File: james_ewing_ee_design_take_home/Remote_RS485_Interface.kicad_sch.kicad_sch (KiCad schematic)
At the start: 16 parts, among them J1 USB_B_Micro, J3 RJ45, U2 MCP2200-E-SS, U3 SN65176BDR, Y1 Resonator

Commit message: Updated
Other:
- note added: "Terminating Resistor"
- title: (none) -> Remote Interface Communication Circuit
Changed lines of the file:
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@@
 (kicad_sch (version 20230121) (generator eeschema)
   (paper "A4")
+  (title_block
+    (title "Remote Interface Communication Circuit")
+  )
   (junction (at 68.58 124.46) (diameter 0) (color 0 0 0 0)
   )
@@
     (stroke (width 0) (type default))
   )
+  (text "Terminating \nResistor" (at 123.19 152.4 0)
+    (effects (font (size 1.27 1.27)) (justify left bottom))
+  )
   (text "USB to UART Interface" (at 36.83 27.94 0)

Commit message: Updated Schematic
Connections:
- net 5V  renamed 5V_RI
- no-connect marks 8 -> 17
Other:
- note added: "TODO: Look into Reset Button Circuit for ESP8266"
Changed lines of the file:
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@@
   (junction (at 119.38 139.7) (diameter 0) (color 0 0 0 0)
   )
+  (no_connect (at 129.54 49.53))
   (no_connect (at 137.16 137.16))
   (no_connect (at 38.1 71.12))
   (no_connect (at 48.26 66.04))
+  (no_connect (at 129.54 64.77))
+  (no_connect (at 129.54 57.15))
   (no_connect (at 137.16 134.62))
+  (no_connect (at 129.54 52.07))
+  (no_connect (at 129.54 69.85))
   (no_connect (at 137.16 127))
   (no_connect (at 137.16 139.7))
   (no_connect (at 137.16 132.08))
+  (no_connect (at 129.54 46.99))
+  (no_connect (at 129.54 62.23))
+  (no_connect (at 129.54 67.31))
   (no_connect (at 137.16 129.54))
+  (no_connect (at 129.54 54.61))
   (wire (pts (xy 125.73 139.7) (xy 134.62 139.7))
     (stroke (width 0) (type default))
@@
     (stroke (width 0) (type default))
   )
+  (wire (pts (xy 130.81 59.69) (xy 129.54 59.69))
+    (stroke (width 0) (type default))
+  )
   (wire (pts (xy 74.93 146.05) (xy 69.85 146.05))
     (stroke (width 0) (type default))
@@
     (stroke (width 0) (type default))
   )
+  (wire (pts (xy 82.55 72.39) (xy 83.82 72.39))
+    (stroke (width 0) (type default))
+  )
   (wire (pts (xy 119.38 130.81) (xy 119.38 139.7))
     (stroke (width 0) (type default))
@@
     (stroke (width 0) (type default))
   )
+  (wire (pts (xy 132.08 74.93) (xy 129.54 74.93))
+    (stroke (width 0) (type default))
+  )
   (wire (pts (xy 72.39 48.26) (xy 72.39 46.99))
     (stroke (width 0) (type default))
@@
     (stroke (width 0) (type default))
   )
+  (wire (pts (xy 132.08 72.39) (xy 129.54 72.39))
+    (stroke (width 0) (type default))
+  )
   (wire (pts (xy 80.01 52.07) (xy 83.82 52.07))
+    (stroke (width 0) (type default))
+  )
+  (wire (pts (xy 82.55 77.47) (xy 83.82 77.47))
     (stroke (width 0) (type default))
   )
@@
     (effects (font (size 1.27 1.27)) (justify left bottom))
   )
+  (text "TODO: Look into Reset Button Circuit for ESP8266" (at 162.56 69.85 0)
+    (effects (font (size 1.27 1.27)) (justify left bottom))
+  )
   (text "12MHz Resonator for USB" (at 45.72 41.91 0)
     (effects (font (size 1.27 1.27)) (justify left bottom))
@@
     (effects (font (size 1.27 1.27)) (justify left bottom))
   )
-  (global_label "TX_RX_SEL" (shape input) (at 129.54 59.69 0) (fields_autoplaced)
+  (label "D_Plus" (at 48.26 60.96 0) (fields_autoplaced)
+    (effects (font (size 1.27 1.27)) (justify left bottom))
+  )
+  (label "D_Minus" (at 82.55 72.39 180) (fields_autoplaced)
+    (effects (font (size 1.27 1.27)) (justify right bottom))
+  )
+  (label "UART_TX" (at 55.88 151.13 180) (fields_autoplaced)
+    (effects (font (size 1.27 1.27)) (justify right bottom))
+  )
+  (label "D_Minus" (at 48.26 63.5 0) (fields_autoplaced)
+    (effects (font (size 1.27 1.27)) (justify left bottom))
+  )
+  (label "D_Plus" (at 82.55 77.47 180) (fields_autoplaced)
+    (effects (font (size 1.27 1.27)) (justify right bottom))
+  )
+  (label "TX_RX_SEL" (at 130.81 59.69 0) (fields_autoplaced)
+    (effects (font (size 1.27 1.27)) (justify left bottom))
+  )
+  (label "UART_TX" (at 132.08 72.39 0) (fields_autoplaced)
+    (effects (font (size 1.27 1.27)) (justify left bottom))
+  )
+  (label "UART_RX" (at 132.08 74.93 0) (fields_autoplaced)
+    (effects (font (size 1.27 1.27)) (justify left bottom))
+  )
+  (label "TX_RX_SEL" (at 58.42 146.05 180) (fields_autoplaced)
+    (effects (font (size 1.27 1.27)) (justify right bottom))
+  )
+  (label "UART_RX" (at 55.88 140.97 180) (fields_autoplaced)
+    (effects (font (size 1.27 1.27)) (justify right bottom))
+  )
+  (global_label "5V_RI" (shape input) (at 85.09 121.92 90) (fields_autoplaced)
     (effects (font (size 1.27 1.27)) (justify left))
-    (property "Intersheetrefs" "${INTERSHEET_REFS}" (at 142.5036 59.69 0)
+    (property "Intersheetrefs" "${INTERSHEET_REFS}" (at 85.09 113.7943 90)
       (effects (font (size 1.27 1.27)) (justify left) hide)
     )
   )
-  (global_label "D_Minus" (shape input) (at 83.82 72.39 180) (fields_autoplaced)
+  (global_label "5V_RI" (shape input) (at 109.22 93.98 270) (fields_autoplaced)
     (effects (font (size 1.27 1.27)) (justify right))
-    (property "Intersheetrefs" "${INTERSHEET_REFS}" (at 73.2149 72.39 0)
+    (property "Intersheetrefs" "${INTERSHEET_REFS}" (at 109.22 102.1057 90)
       (effects (font (size 1.27 1.27)) (justify right) hide)
     )
   )
-  (global_label "5V " (shape input) (at 85.09 121.92 90) (fields_autoplaced)
+  (global_label "5V_RI" (shape input) (at 48.26 55.88 0) (fields_autoplaced)
     (effects (font (size 1.27 1.27)) (justify left))
-    (property "Intersheetrefs" "${INTERSHEET_REFS}" (at 85.09 115.6691 90)
+    (property "Intersheetrefs" "${INTERSHEET_REFS}" (at 56.3857 55.88 0)
       (effects (font (size 1.27 1.27)) (justify left) hide)
     )
-  )
-  (global_label "D_Plus" (shape input) (at 83.82 77.47 180) (fields_autoplaced)
-    (effects (font (size 1.27 1.27)) (justify right))
-    (property "Intersheetrefs" "${INTERSHEET_REFS}" (at 74.4849 77.47 0)
-      (effects (font (size 1.27 1.27)) (justify right) hide)
-    )
-  )
-  (global_label "UART_TX" (shape output) (at 129.54 72.39 0) (fields_autoplaced)
-    (effects (font (size 1.27 1.27)) (justify left))
-    (property "Intersheetrefs" "${INTERSHEET_REFS}" (at 140.3266 72.39 0)
-      (effects (font (size 1.27 1.27)) (justify left) hide)
-    )
-  )
-  (global_label "D_Minus" (shape input) (at 48.26 63.5 0) (fields_autoplaced)
-    (effects (font (size 1.27 1.27)) (justify left))
-    (property "Intersheetrefs" "${INTERSHEET_REFS}" (at 58.8651 63.5 0)
-      (effects (font (size 1.27 1.27)) (justify left) hide)
-    )
-  )
-  (global_label "UART_RX" (shape output) (at 55.88 140.97 180) (fields_autoplaced)
-    (effects (font (size 1.27 1.27)) (justify right))
-    (property "Intersheetrefs" "${INTERSHEET_REFS}" (at 44.791 140.97 0)
-      (effects (font (size 1.27 1.27)) (justify right) hide)
-    )
-  )
-  (global_label "5V " (shape input) (at 109.22 93.98 270) (fields_autoplaced)
-    (effects (font (size 1.27 1.27)) (justify right))
-    (property "Intersheetrefs" "${INTERSHEET_REFS}" (at 109.22 100.2309 90)
-      (effects (font (size 1.27 1.27)) (justify right) hide)
-    )
-  )
-  (global_label "UART_RX" (shape input) (at 129.54 74.93 0) (fields_autoplaced)
-    (effects (font (size 1.27 1.27)) (justify left))
-    (property "Intersheetrefs" "${INTERSHEET_REFS}" (at 140.629 74.93 0)
-      (effects (font (size 1.27 1.27)) (justify left) hide)
-    )
-  )
-  (global_label "TX_RX_SEL" (shape input) (at 58.42 146.05 180) (fields_autoplaced)
-    (effects (font (size 1.27 1.27)) (justify right))
-    (property "Intersheetrefs" "${INTERSHEET_REFS}" (at 45.4564 146.05 0)
-      (effects (font (size 1.27 1.27)) (justify right) hide)
-    )
-  )
-  (global_label "UART_TX" (shape input) (at 55.88 151.13 180) (fields_autoplaced)
-    (effects (font (size 1.27 1.27)) (justify right))
-    (property "Intersheetrefs" "${INTERSHEET_REFS}" (at 45.0934 151.13 0)
-      (effects (font (size 1.27 1.27)) (justify right) hide)
-    )
-  )
-  (global_label "5V " (shape input) (at 48.26 55.88 0) (fields_autoplaced)
-    (effects (font (size 1.27 1.27)) (justify left))
-    (property "Intersheetrefs" "${INTERSHEET_REFS}" (at 54.5109 55.88 0)
-      (effects (font (size 1.27 1.27)) (justify left) hide)
-    )
-  )
-  (global_label "D_Plus" (shape input) (at 48.26 60.96 0) (fields_autoplaced)
-    (effects (font (size 1.27 1.27)) (justify left))
-    (property "Intersheetrefs" "${INTERSHEET_REFS}" (at 57.5951 60.96 0)
-      (effects (font (size 1.27 1.27)) (justify left) hide)
-    )

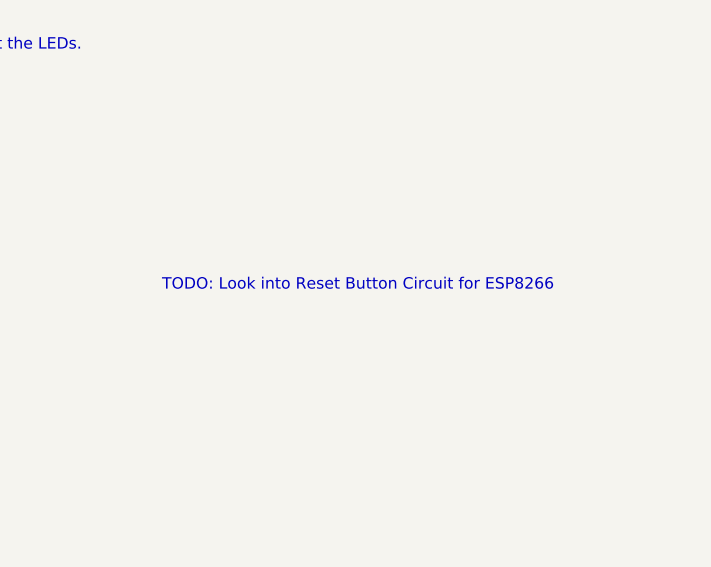
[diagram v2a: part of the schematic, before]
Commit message: Updates to Node Labeling
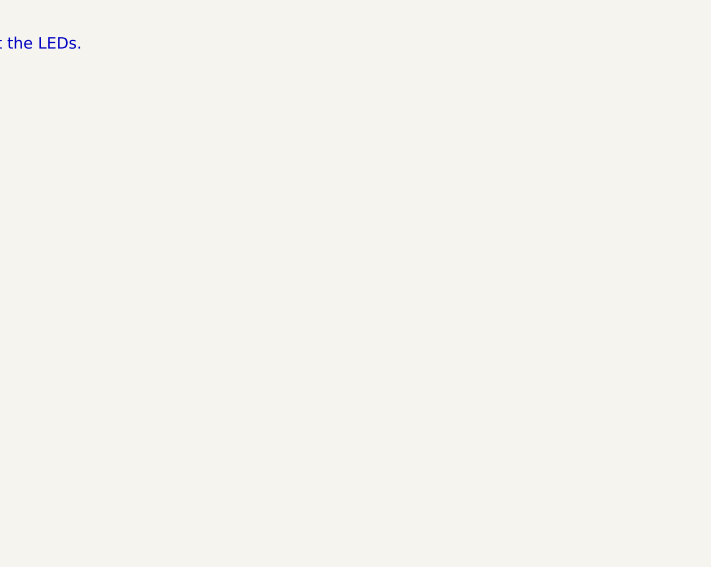
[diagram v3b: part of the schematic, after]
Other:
- note removed: "TODO: Look into Reset Button Circuit for ESP8266"
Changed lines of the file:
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@@
-    (effects (font (size 1.27 1.27)) (justify left bottom))
-  )
-  (text "TODO: Look into Reset Button Circuit for ESP8266" (at 162.56 69.85 0)
     (effects (font (size 1.27 1.27)) (justify left bottom))
   )
